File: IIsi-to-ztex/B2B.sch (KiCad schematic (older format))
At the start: 8 parts, among them J1 Conn_02x07_Odd_Even

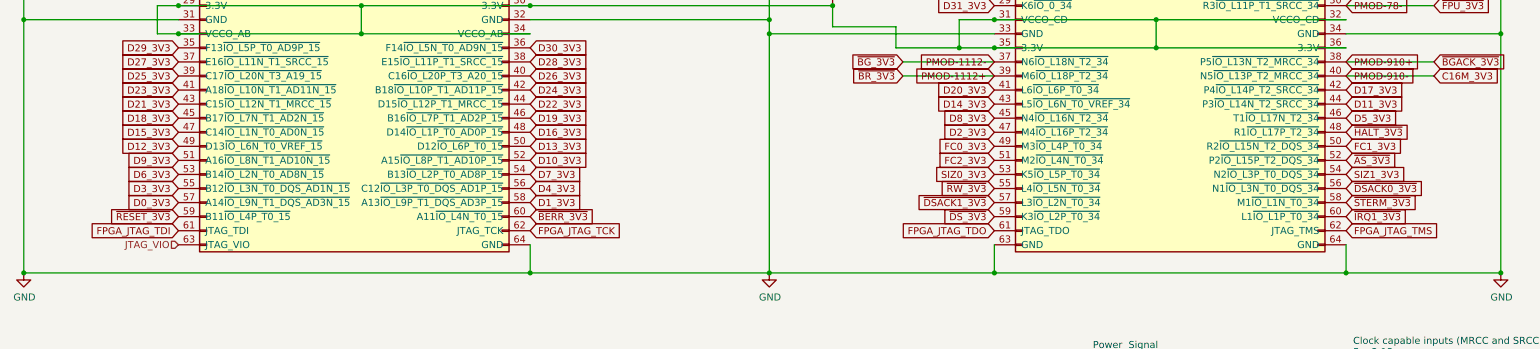
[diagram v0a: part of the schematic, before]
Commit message: rework /HALT
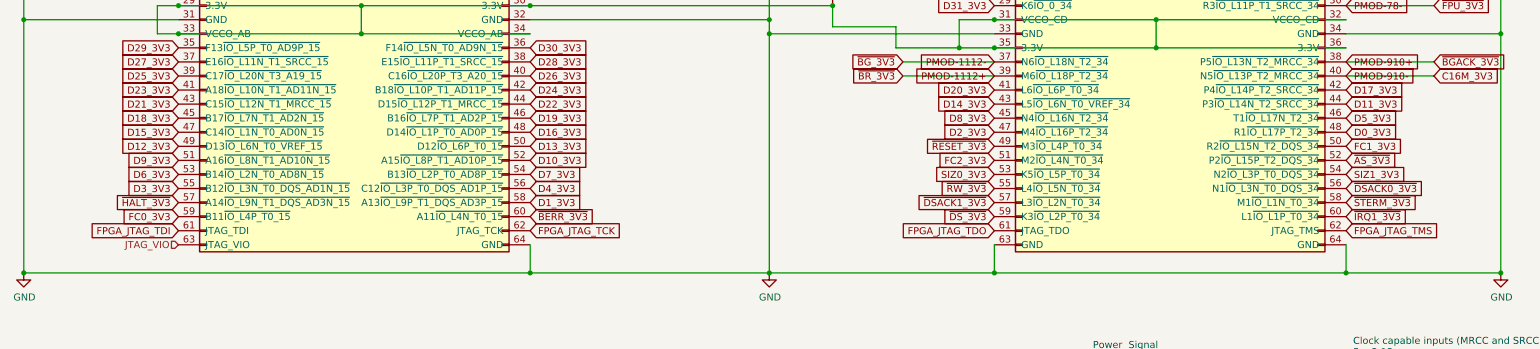
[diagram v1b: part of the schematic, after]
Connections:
- net D0_3V3: now also JCD1.48 (R1~IO_L17P_T2_34); no longer JAB1.57 (A14~IO_L9N_T1_DQS_AD3N_15)
- net FC0_3V3: now also JAB1.59 (B11~IO_L4P_T0_15); no longer JCD1.49 (M3~IO_L4P_T0_34)
- net ~HALT_3V3: now also JAB1.57 (A14~IO_L9N_T1_DQS_AD3N_15); no longer JCD1.48 (R1~IO_L17P_T2_34)
- net ~RESET_3V3: now also JCD1.49 (M3~IO_L4P_T0_34); no longer JAB1.59 (B11~IO_L4P_T0_15)
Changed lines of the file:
@@
 Text GLabel 7400 3750 0    50   Input ~ 0
 SIZ0_3V3
+Text GLabel 1600 3950 0    50   Input ~ 0
+~HALT_3V3
 Text GLabel 9900 3450 2    50   Input ~ 0
-~HALT_3V3
-Text GLabel 1600 3950 0    50   Input ~ 0
 D0_3V3
 Text GLabel 4100 4050 2    50   Input ~ 0
 ~BERR_3V3
-Text GLabel 1600 4050 0    50   Input ~ 0
+Text GLabel 7400 3550 0    50   Input ~ 0
 ~RESET_3V3
 Text GLabel 9900 3550 2    50   Input ~ 0
@@
 Text GLabel 7400 3650 0    50   Input ~ 0
 FC2_3V3
-Text GLabel 7400 3550 0    50   Input ~ 0
+Text GLabel 1600 4050 0    50   Input ~ 0
 FC0_3V3
 Text GLabel 9900 3650 2    50   Input ~ 0

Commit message: cleanup DRC
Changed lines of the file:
@@
 Wire Wire Line
 	9900 2550 10525 2550
+Text GLabel 10525 2250 2    50   Input ~ 0
+~IRQ3_3V3
+Text GLabel 10525 2350 2    50   Input ~ 0
+~IRQ2_3V3
+Wire Wire Line
+	9900 2350 10525 2350
+Wire Wire Line
+	10525 2250 9900 2250
 $EndSCHEMATC

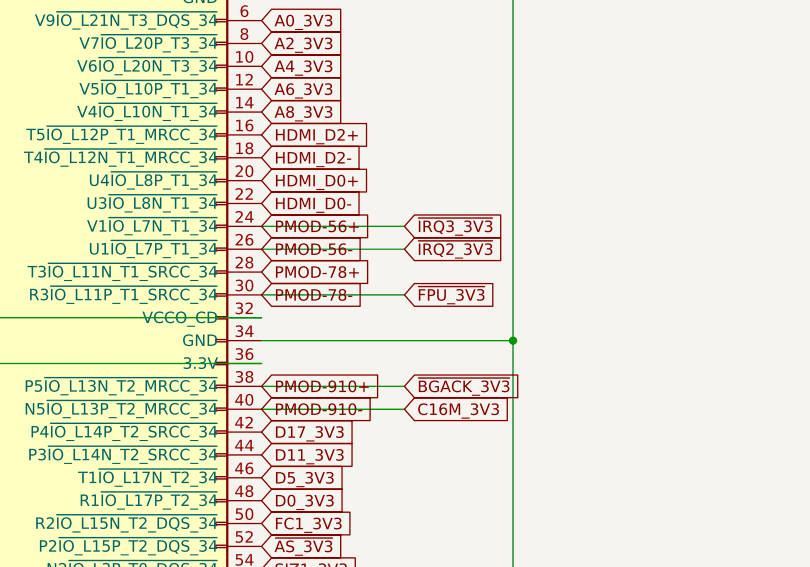
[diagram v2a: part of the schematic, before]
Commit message: connect rbv to last pmod pin
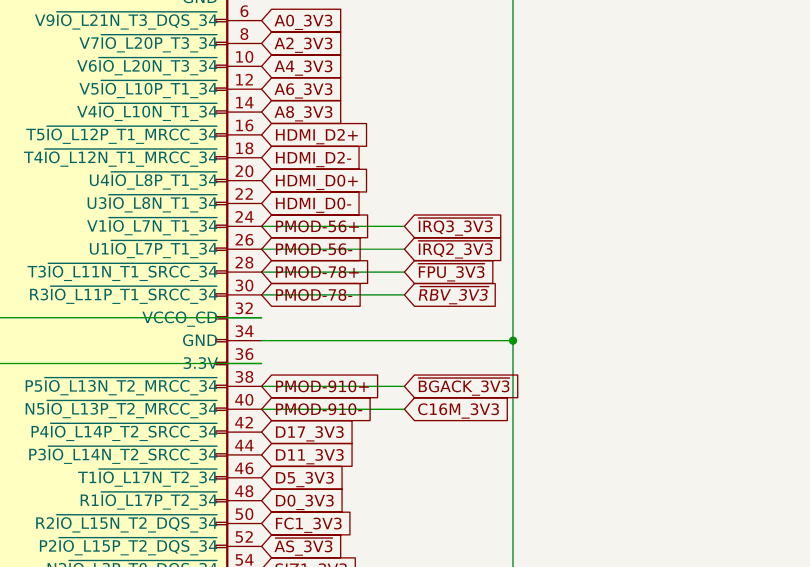
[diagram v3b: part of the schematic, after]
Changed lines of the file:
@@
 Text GLabel 6750 3050 0    50   Input ~ 0
 ~BR_3V3
-Text GLabel 10525 2550 2    50   Input ~ 0
+Text GLabel 10525 2450 2    50   Input ~ 0
 ~FPU_3V3
 Wire Wire Line
@@
 Wire Wire Line
 	10525 2250 9900 2250
+Text GLabel 10525 2550 2    50   Input Italic 0
+~RBV_3V3
+Wire Wire Line
+	10525 2450 9900 2450
 $EndSCHEMATC
